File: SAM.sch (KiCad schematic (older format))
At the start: 44 parts

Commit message: moved a bunch of things around inside the schematics
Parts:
- added TP?: TP, tm-kicad-lib:Testpoint, symbol TP
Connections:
- wire segments 186 -> 188
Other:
- moved on the sheet: TP?
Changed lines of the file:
@@
 	14500 6600 13700 6600
 Wire Wire Line
-	2600 6100 3500 6100
+	2400 6100 3500 6100
 Wire Wire Line
 	3500 6100 3500 6200
@@
 	3700 6800 3050 6800
 Wire Wire Line
-	2500 7200 3700 7200
-Wire Wire Line
-	2400 7300 3700 7300
-Wire Wire Line
-	2300 7400 3700 7400
-Wire Wire Line
-	2100 7500 3700 7500
-Wire Wire Line
-	3700 7700 1800 7700
-Wire Wire Line
-	2300 7800 3700 7800
-Wire Wire Line
-	2400 7900 3700 7900
-Wire Wire Line
-	2500 8000 3700 8000
+	2300 7200 3700 7200
+Wire Wire Line
+	2200 7300 3700 7300
+Wire Wire Line
+	2100 7400 3700 7400
+Wire Wire Line
+	1900 7500 3700 7500
+Wire Wire Line
+	3700 7700 1600 7700
+Wire Wire Line
+	2100 7800 3700 7800
+Wire Wire Line
+	2200 7900 3700 7900
+Wire Wire Line
+	2300 8000 3700 8000
 Text GLabel 3050 6350 0    60   Input ~ 0
 I_USB0
@@
 Text GLabel 3300 7050 0    60   Input ~ 0
 5V_DIV_BUFF
-Text GLabel 2100 7350 0    60   Input ~ 0
+Text GLabel 1900 7350 0    60   Input ~ 0
 33MT_DIV_BUFF
-Text GLabel 2100 7500 0    60   Input ~ 0
+Text GLabel 1900 7500 0    60   Input ~ 0
 33CP_DIV_BUFF
 Text Label 6600 8800 0    60   ~ 0
@@
 	3500 7050 3300 7050
 Wire Wire Line
-	2500 7200 2500 7050
-Wire Wire Line
-	2500 7050 2200 7050
-Wire Wire Line
-	2200 7200 2400 7200
-Wire Wire Line
-	2400 7200 2400 7300
-Wire Wire Line
-	2300 7400 2300 7350
-Wire Wire Line
-	2300 7350 2100 7350
-Wire Wire Line
-	2300 7800 2300 7850
-Wire Wire Line
-	2300 7850 1800 7850
+	2300 7200 2300 7050
+Wire Wire Line
+	2300 7050 2000 7050
+Wire Wire Line
+	2000 7200 2200 7200
+Wire Wire Line
+	2200 7200 2200 7300
+Wire Wire Line
+	2100 7400 2100 7350
+Wire Wire Line
+	2100 7350 1900 7350
+Wire Wire Line
+	2100 7800 2100 7850
+Wire Wire Line
+	2100 7850 1600 7850
 $Comp
 L TP TP?
@@
 L TP TP?
 U 1 1 553FFED4
-P 7600 8600
-F 0 "TP?" H 7600 8650 60  0000 C CNN
-F 1 "TP" H 7600 8550 60  0001 C CNN
-F 2 "tm-kicad-lib:Testpoint" H 7600 8600 60  0001 C CNN
-F 3 "" H 7600 8600 60  0000 C CNN
-	1    7600 8600
-	1    0    0    -1
+P 2400 6100
+F 0 "TP?" H 2400 6150 60  0000 C CNN
+F 1 "TP" H 2400 6050 60  0001 C CNN
+F 2 "tm-kicad-lib:Testpoint" H 2400 6100 60  0001 C CNN
+F 3 "" H 2400 6100 60  0000 C CNN
+	1    2400 6100
+	-1   0    0    1
 $EndComp
 Text GLabel 6900 5050 2    60   Output ~ 0
@@
 Wire Wire Line
 	6800 5350 6900 5350
-Text GLabel 2200 7050 0    60   Input ~ 0
+Text GLabel 2000 7050 0    60   Input ~ 0
 5VUSB0_DIV_BUFF
-Text GLabel 2200 7200 0    60   Input ~ 0
+Text GLabel 2000 7200 0    60   Input ~ 0
 5VUSB1_DIV_BUFF
-Text GLabel 2100 8150 0    60   Input ~ 0
+Text GLabel 1900 8150 0    60   Input ~ 0
 33PB_DIV_BUFF
-Text GLabel 2100 8000 0    60   Input ~ 0
+Text GLabel 1900 8000 0    60   Input ~ 0
 33PA_DIV_MEAS
-Text GLabel 1800 7850 0    60   Input ~ 0
+Text GLabel 1600 7850 0    60   Input ~ 0
 12_BUFF
-Text GLabel 1800 7700 0    60   Input ~ 0
+Text GLabel 1600 7700 0    60   Input ~ 0
 18_BUFF
 Wire Wire Line
-	2400 7900 2400 8000
-Wire Wire Line
-	2400 8000 2100 8000
-Wire Wire Line
-	2500 8000 2500 8150
-Wire Wire Line
-	2500 8150 2100 8150
+	2200 7900 2200 8000
+Wire Wire Line
+	2200 8000 1900 8000
+Wire Wire Line
+	2300 8000 2300 8150
+Wire Wire Line
+	2300 8150 1900 8150
+$Comp
+L TP TP?
+U 1 1 55403462
+P 2400 6800
+F 0 "TP?" H 2400 6850 60  0000 C CNN
+F 1 "TP" H 2400 6750 60  0001 C CNN
+F 2 "tm-kicad-lib:Testpoint" H 2400 6800 60  0001 C CNN
+F 3 "" H 2400 6800 60  0000 C CNN
+	1    2400 6800
+	-1   0    0    1
+$EndComp
+Wire Wire Line
+	2400 6800 2600 6800
+Wire Wire Line
+	2600 6800 2600 6950
 $EndSCHEMATC

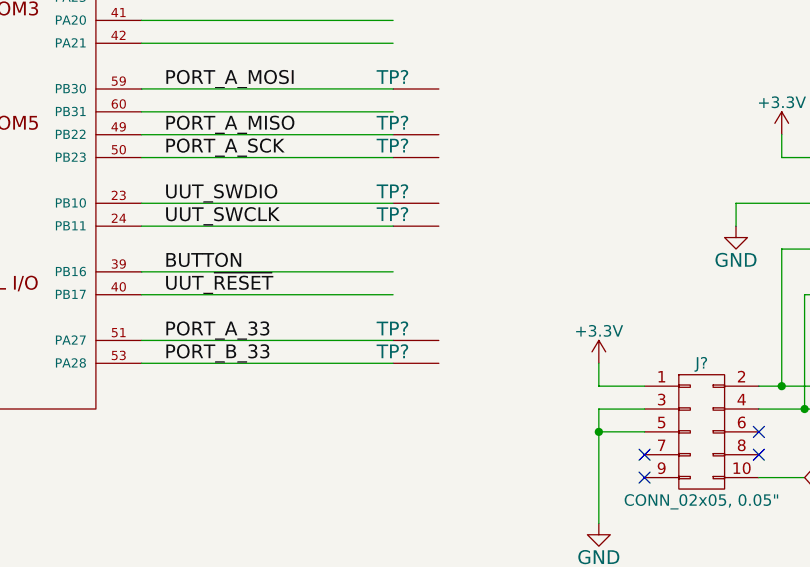
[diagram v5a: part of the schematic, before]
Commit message: schematic check with kevin. misc fixes, mostly on usb
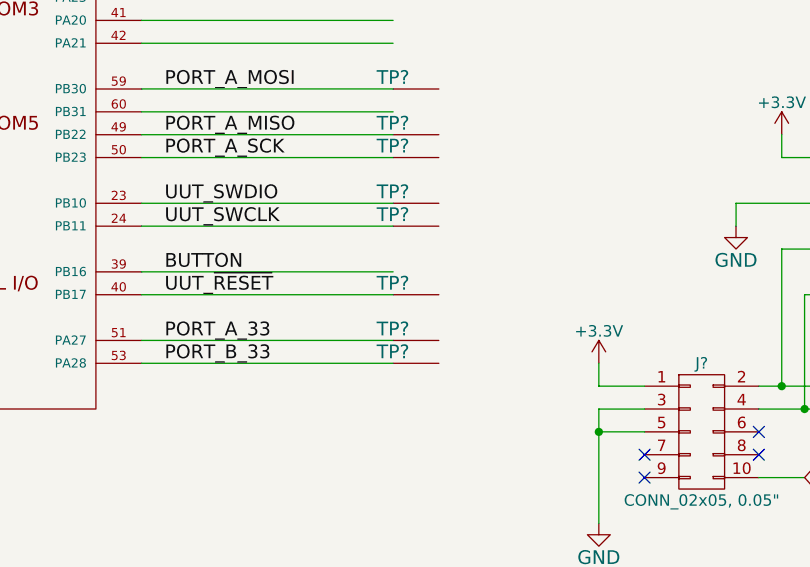
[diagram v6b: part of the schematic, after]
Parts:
- added TP?: TP, tm-kicad-lib:Testpoint, symbol TP
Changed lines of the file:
@@
 Wire Wire Line
 	2600 6800 2600 6950
+$Comp
+L TP TP?
+U 1 1 5542FA8D
+P 7600 8600
+F 0 "TP?" H 7600 8650 60  0000 C CNN
+F 1 "TP" H 7600 8550 60  0001 C CNN
+F 2 "tm-kicad-lib:Testpoint" H 7600 8600 60  0001 C CNN
+F 3 "" H 7600 8600 60  0000 C CNN
+	1    7600 8600
+	1    0    0    -1
+$EndComp
 $EndSCHEMATC

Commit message: passed schematic review
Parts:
- removed C?: 100nF, tm-kicad-lib:SMD-0402-C, symbol TM_C
- removed D?: BLUE, LEDs:LED-0603, symbol LED
- removed R? (x2): 10kR, tm-kicad-lib:SMD-0402-R, symbol TM_R
- removed R?: 1kR, tm-kicad-lib:SMD-0402-R, symbol TM_R
- removed SW?: SW_PUSH, tm-kicad-lib:TL1015AF160QG, symbol SW_PUSH
- removed TP? (x3): TP, tm-kicad-lib:Testpoint, symbol TP
- added C? (x3): 100nF, tm-kicad-lib:SMD-0402-C, symbol TM_C
- added C?: 10uF, tm-kicad-lib:SMD-0805-C, symbol TM_C
- added D?: RED, LEDs:LED-0603, symbol LED
- added D?: YELLOW, LEDs:LED-0603, symbol LED
- added D?: GREEN, LEDs:LED-0603, symbol LED
- added D?: BLUE, LEDs:LED-0603, symbol LED
- added R? (x4): 1kR, tm-kicad-lib:SMD-0402-R, symbol TM_R
- added R? (x6): 10kR, tm-kicad-lib:SMD-0402-R, symbol TM_R
- added R?: 330R, tm-kicad-lib:SMD-0402-R, symbol TM_R
- added R?: 120R, tm-kicad-lib:SMD-0402-R, symbol TM_R
- added SW? (x2): Switch_DPST, symbol Switch_DPST
- added TP?: TP, symbol TP
- added TP?: TP, tm-kicad-lib:Testpoint, symbol TP
- added U? (x2): AAT4610, symbol AAT4610
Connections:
- net labels added: 33PA_DIV_BUFF, BOTH_G3, FAIL_LED, FAIL_MID, I_UUT, PASS_LED, PASS_MID, READY_LED, READY_MID, TEST_IN_PROGRESS_LED, TEST_START_BUTTON, TIP_MID, UUT_5V_UPSTREAM, UUT_VIN, UUT_VINUSB, UUT_~ENABLE~_USB, UUT_~ENABLE~_VIN
- net labels removed: 33PA_DIV_MEAS, BUTTON, PORT_A_33, PORT_B_33
- wire segments 188 -> 246
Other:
- note added: "SWAP: MT9700"
- moved on the sheet: C?, J?, L?, TP?, U?, X?
